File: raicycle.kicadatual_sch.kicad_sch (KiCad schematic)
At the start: 9 parts, among them U1 Adafruit_Feather_ESP32_V2, U2 BME688_1, U3 VL53L0X, U4 Grove_Wio-E5, U5 Air530

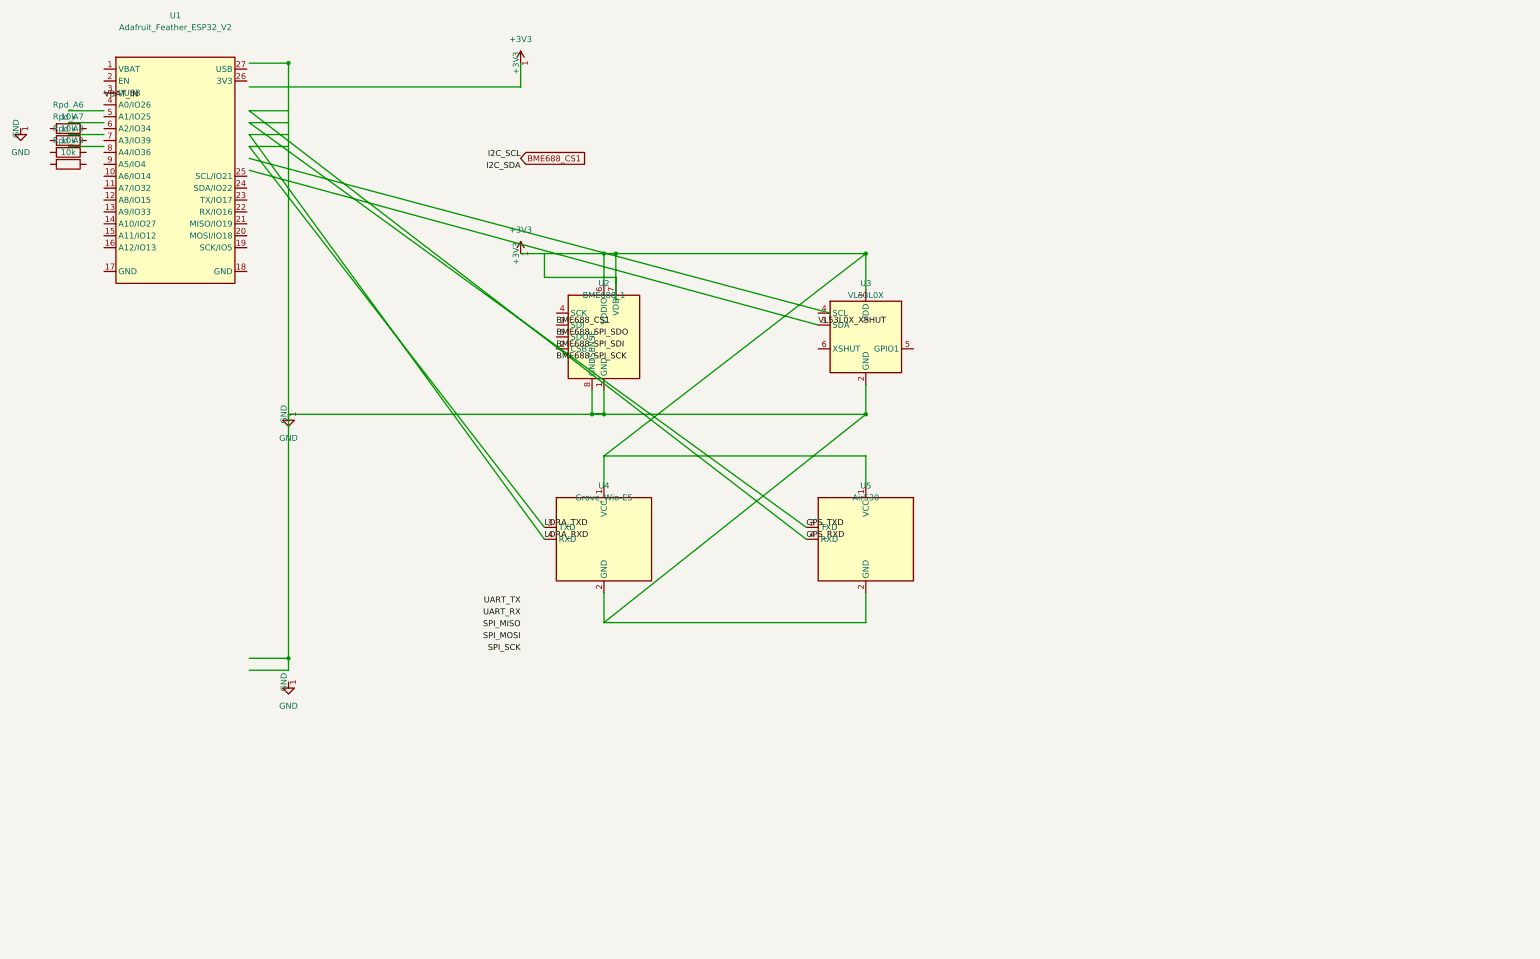
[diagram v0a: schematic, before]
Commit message: Complete KiCad 8.0 schematic with all modifications and 8-sensor BME688 array
Co-authored-by: 968096 <203631091+968096@users.noreply.github.com>
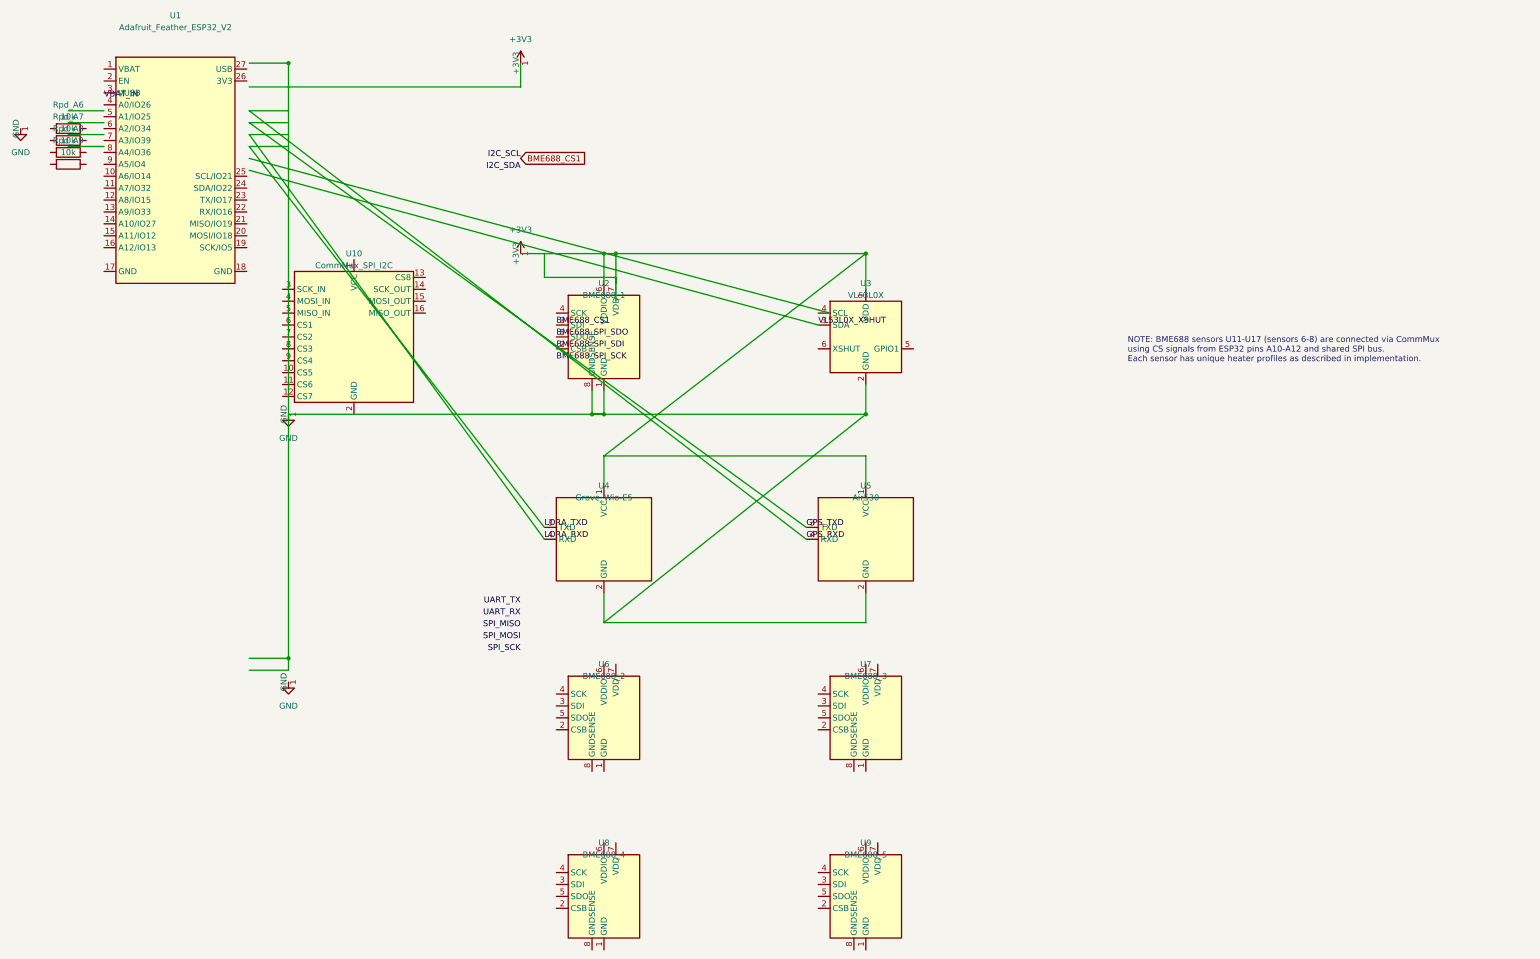
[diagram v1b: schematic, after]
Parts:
- added U10: CommMux_SPI_I2C, symbol Interface_Expansion:CommMux_SPI_I2C
- added U6: BME688_2, Package_LGA:Bosch_LGA-8_3x3mm_P0.8mm, symbol Sensor_Environmental:BME688
- added U7: BME688_3, Package_LGA:Bosch_LGA-8_3x3mm_P0.8mm, symbol Sensor_Environmental:BME688
- added U8: BME688_4, Package_LGA:Bosch_LGA-8_3x3mm_P0.8mm, symbol Sensor_Environmental:BME688
- added U9: BME688_5, Package_LGA:Bosch_LGA-8_3x3mm_P0.8mm, symbol Sensor_Environmental:BME688
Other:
- note added: "NOTE: BME688 sensors U11-U17 (sensors 6-8) are connected via CommMux using CS signals from ESP32 pins A10-A12 and shared SPI bus. Each sensor has unique heater profiles as described in implementation."
